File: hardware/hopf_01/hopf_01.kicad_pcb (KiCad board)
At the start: 2 copper layers, 120.2 x 120.2 mm, 257 parts, among them J1 SMA_50R, J2 SMA_50R, J3 SMA_50R, J4 SMA_50R

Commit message: updated table
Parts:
- moved ? 67.9 mm to (139.6, 69.5)
- moved ? 67.9 mm to (88.1, 117.0)
- moved ? 67.9 mm to (94.6, 128.8)
- moved ? 67.9 mm to (146.6, 74.1)
- moved ? 67.9 mm to (86.7, 62.9)
- moved ? 67.9 mm to (91.7, 56.4)
- moved ? 67.9 mm to (80.4, 72.0)
- moved ? 67.9 mm to (136.9, 117.2)
- moved ? 67.9 mm to (154.2, 56.5)
- moved ? 67.9 mm to (81.3, 74.8)
- moved ? 67.9 mm to (88.9, 55.4)
- moved ? 67.9 mm to (80.4, 61.9)
- moved ? 67.9 mm to (148.9, 114.2)
- moved ? 67.9 mm to (157.9, 125.5)
- moved ? 67.9 mm to (84.7, 123.9)
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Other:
- board size 120.2 x 120.2 mm -> 120 x 120 mm

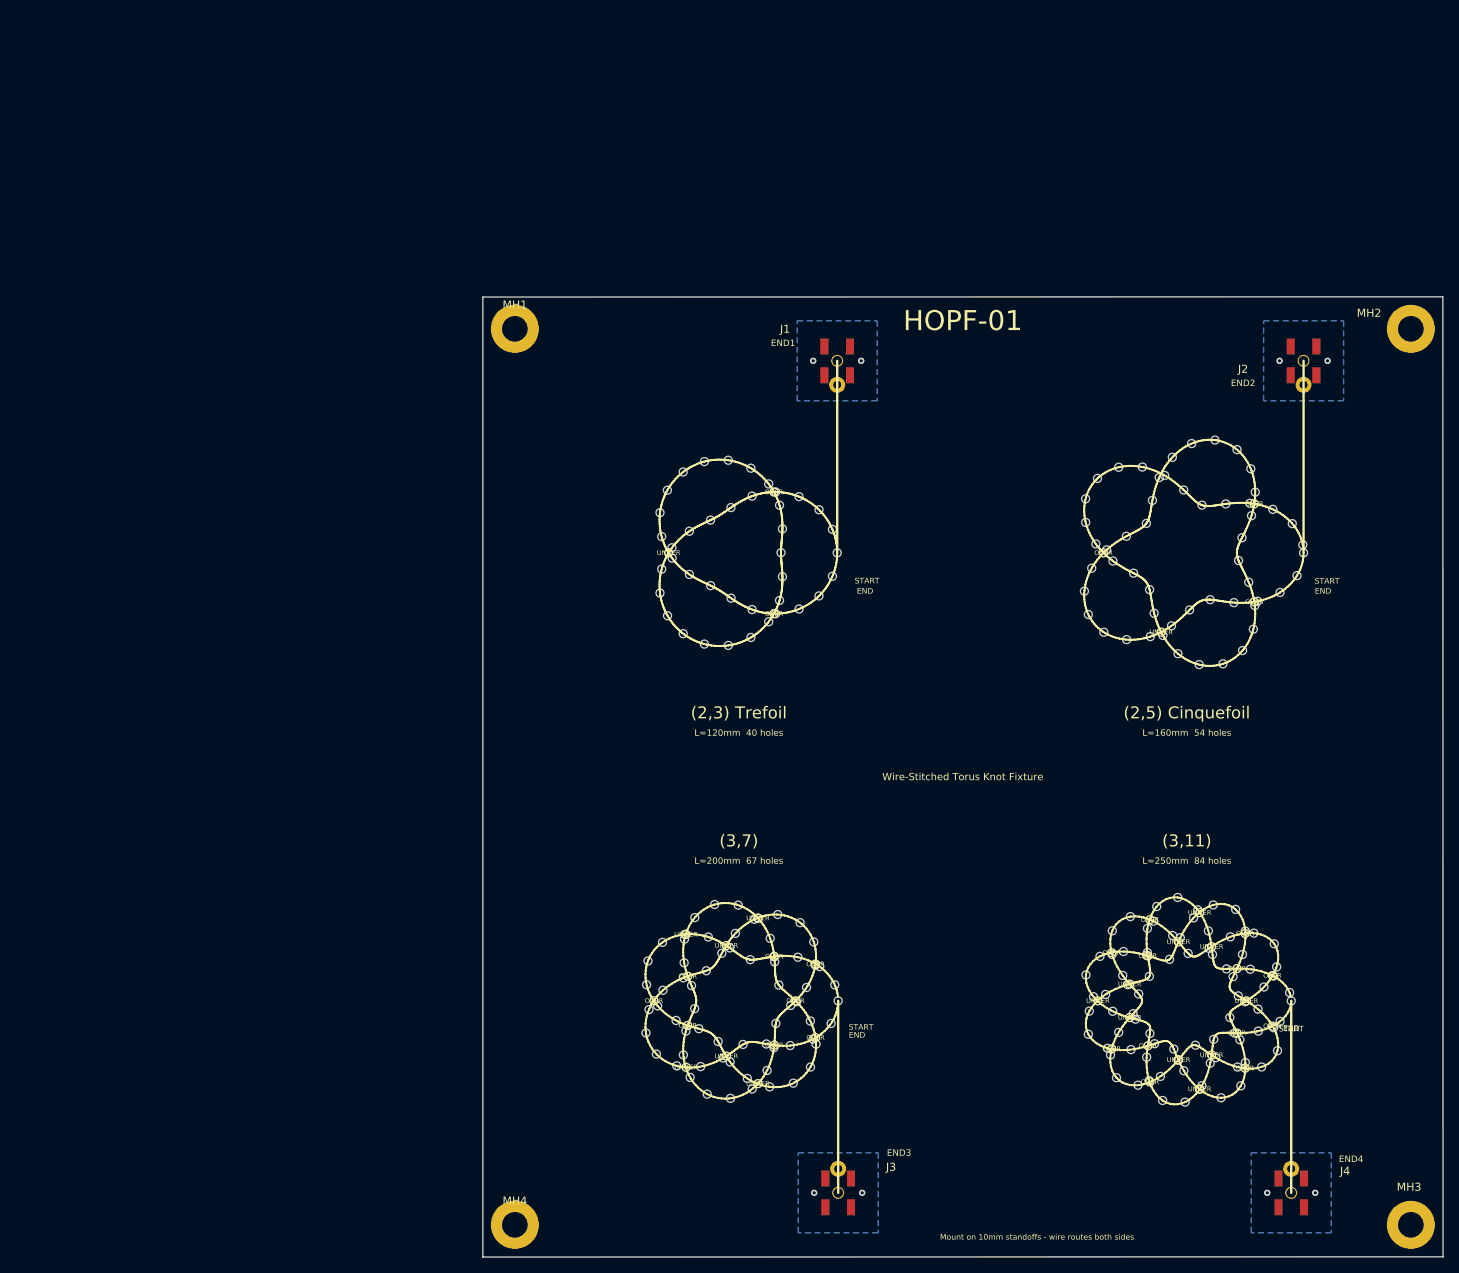
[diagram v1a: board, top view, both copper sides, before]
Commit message: updated PCB trace experiment
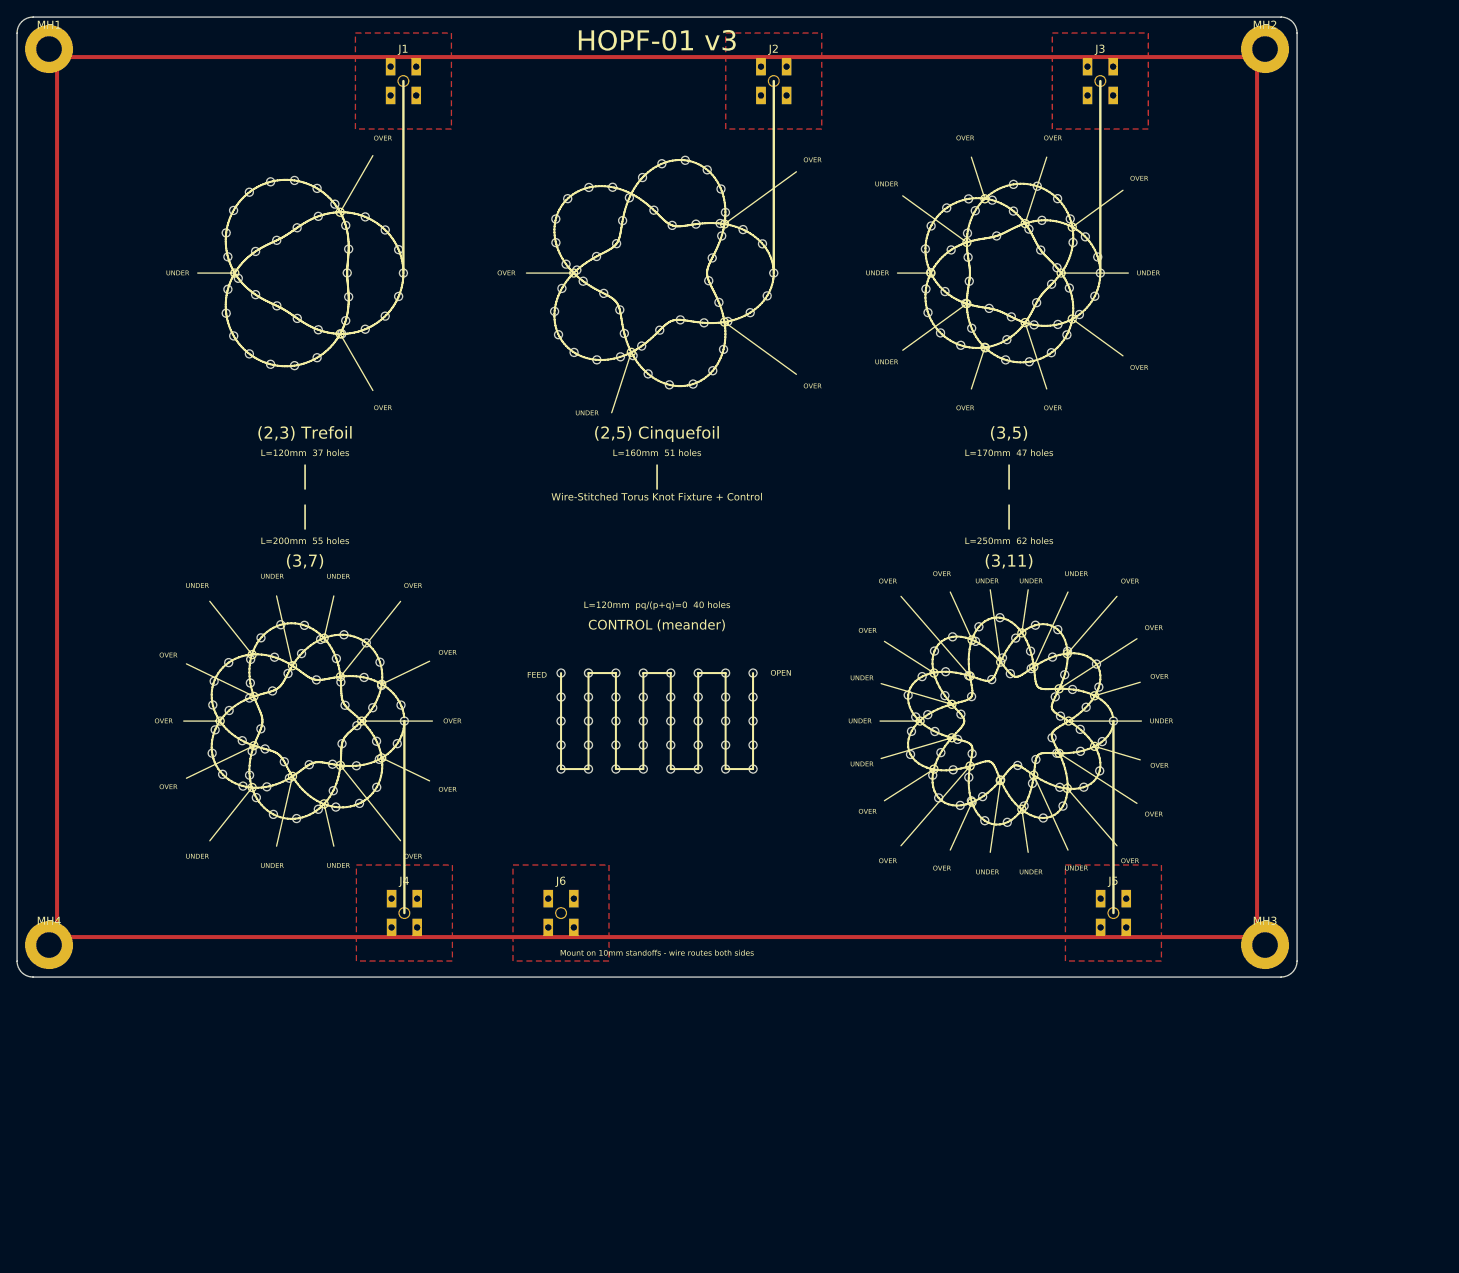
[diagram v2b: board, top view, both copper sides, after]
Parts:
- removed the ? at (139.6, 69.5)
- removed the ? at (88.1, 117.0)
- removed the ? at (83.6, 126.7)
- removed the ? at (101.9, 64.0)
- removed the ? at (94.6, 128.8)
- removed the ? at (149.8, 130.1)
- removed the ? at (137.7, 126.9)
- removed the ? at (145.9, 131.7)
- removed the ? at (146.6, 74.1)
- removed the ? at (86.7, 62.9)
- removed the ? at (96.6, 128.6)
- removed the ? at (91.7, 56.4)
- removed the ? at (144.5, 114.8)
- removed the ? at (80.4, 72.0)
- removed the ? at (142.9, 132.4)
- removed the ? at (136.9, 117.2)
- removed the ? at (154.2, 56.5)
- removed the ? at (78.7, 121.0)
- removed the ? at (81.3, 74.8)
- removed the ? at (79.0, 124.1)
- removed the ? at (88.9, 55.4)
- removed the ? at (80.4, 61.9)
- removed the ? at (148.9, 114.2)
- removed the ? at (157.9, 125.5)
- removed the ? at (94.8, 125.8)
- removed the ? at (84.7, 123.9)
- removed the ? at (83.4, 118.2)
- removed the ? at (144.4, 55.0)
- removed the ? at (145.8, 59.1)
- removed the ? at (149.1, 72.8)
- removed the ? at (85.2, 126.5)
- removed the ? at (101.9, 69.9)
- removed the ? at (83.3, 77.1)
- removed the ? at (155.1, 73.0)
- removed the ? at (89.8, 114.5)
- removed the ? at (155.9, 121.2)
- removed the ? at (84.0, 69.7)
- removed the ? at (86.3, 134.6)
- removed the ? at (84.0, 64.3)
- removed the ? at (157.0, 61.5)
- removed the ? at (136.3, 128.9)
- removed the ? at (157.6, 129.2)
- removed the ? at (85.9, 55.6)
- removed the ? at (141.6, 127.1)
- removed the ? at (145.1, 130.4)
- removed the ? at (141.5, 132.9)
- removed the ? at (95.7, 69.9)
- removed the ? at (93.7, 128.4)
- removed the ? at (151.1, 60.9)
- removed the ? at (145.4, 115.1)
- removed the ? at (99.8, 118.5)
- removed the ? at (94.6, 117.4)
- removed the ? at (138.7, 64.9)
- removed the ? at (155.2, 126.8)
- removed the ? at (97.7, 74.0)
- removed the ? at (133.6, 119.7)
- removed the ? at (154.2, 119.0)
- removed the ? at (138.7, 77.8)
- removed the ? at (99.5, 127.8)
- removed the ? at (133.4, 71.8)
- removed the ? at (152.5, 54.1)
- removed the ? at (141.2, 63.3)
- removed the ? at (153.5, 130.7)
- removed the ? at (153.5, 123.1)
- removed the ? at (94.8, 59.4)
- removed the ? at (83.3, 129.7)
- removed the ? at (83.5, 114.7)
- removed the ? at (141.2, 130.0)
- removed the ? at (80.7, 115.7)
- removed the ? at (135.1, 57.7)
- removed the ? at (91.9, 74.1)
- removed the ? at (136.2, 66.6)
- removed the ? at (86.2, 119.2)
- removed the ? at (153.5, 114.3)
- removed the ? at (101.8, 125.8)
- removed the ? at (97.7, 59.9)
- removed the ? at (152.1, 73.2)
- removed the ? at (99.9, 128.4)
- removed the ? at (141.3, 116.9)
- removed the ? at (136.9, 114.2)
- removed the ? at (155.6, 131.2)
- removed the ? at (139.8, 125.3)
- removed the ? at (155.1, 124.0)
- removed the ? at (95.3, 61.0)
- removed the ? at (80.6, 69.0)
- removed the ? at (139.2, 129.1)
- removed the ? at (79.9, 129.6)
- removed the ? at (91.9, 134.0)
- removed the ? at (100.2, 72.4)
- removed the ? at (145.1, 110.0)
- removed the ? at (144.6, 129.0)
- removed the ? at (89.1, 116.4)
- removed the ? at (153.2, 117.2)
- removed the ? at (137.7, 56.3)
- removed the ? at (153.2, 79.2)
- removed the ? at (90.1, 111.0)
- removed the ? at (149.4, 117.2)
- removed the ? at (95.2, 121.0)
- removed the ? at (151.2, 119.0)
- removed the ? at (133.6, 63.2)
- removed the ? at (160.7, 66.0)
- removed the ? at (89.3, 72.6)
- removed the ? at (138.2, 119.8)
- removed the ? at (100.2, 61.6)
- removed the ? at (133.9, 127.1)
- removed the ? at (95.1, 112.2)
- removed the ? at (93.8, 131.7)
- removed the ? at (145.1, 79.6)
- removed the ? at (84.3, 121.1)
- removed the ? at (154.8, 59.4)
- removed the ? at (149.0, 116.4)
- removed the ? at (83.3, 56.9)
- removed the ? at (87.6, 128.1)
- removed the ? at (135.4, 117.4)
- removed the ? at (148.1, 61.0)
- removed the ? at (80.6, 64.9)
- removed the ? at (150.5, 135.1)
- removed the ? at (140.1, 133.5)
- removed the ? at (149.2, 130.8)
- removed the ? at (160.8, 67.0)
- removed the ? at (98.7, 121.3)
- removed the ? at (146.0, 135.6)
- removed the ? at (136.7, 129.7)
- removed the ? at (80.1, 123.6)
- removed the ? at (146.8, 53.3)
- removed the ? at (159.1, 121.9)
- removed the ? at (137.0, 124.3)
- removed the ? at (92.2, 112.8)
- removed the ? at (153.1, 65.1)
- removed the ? at (94.8, 74.6)
- removed the ? at (147.8, 80.9)
- removed the ? at (143.2, 135.4)
- removed the ? at (141.3, 113.9)
- removed the ? at (81.9, 67.6)
- removed the ? at (94.7, 118.1)
- removed the ? at (142.8, 57.6)
- removed the ? at (97.0, 133.3)
- removed the ? at (88.9, 78.5)
- removed the ? at (134.6, 122.5)
- removed the ? at (137.0, 68.0)
- removed the ? at (142.2, 128.3)
- removed the ? at (147.3, 128.5)
- removed the ? at (84.1, 132.5)
- removed the ? at (89.1, 130.6)
- removed the ? at (99.2, 125.5)
- removed the ? at (140.2, 122.1)
- removed the ? at (96.7, 123.5)
- removed the ? at (142.0, 113.0)
- removed the ? at (152.2, 127.0)
- removed the ? at (154.6, 114.5)
- removed the ? at (141.9, 60.4)
- removed the ? at (81.9, 66.3)
- removed the ? at (139.2, 112.4)
- removed the ? at (97.6, 117.5)
- removed the ? at (84.7, 112.6)
- removed the ? at (157.2, 115.8)
- removed the ? at (82.4, 125.4)
- removed the ? at (154.5, 76.5)
- removed the ? at (136.1, 122.2)
- removed the ? at (94.0, 58.4)
- removed the ? at (152.0, 119.9)
- removed the ? at (150.7, 80.8)
- removed the ? at (91.3, 132.7)
- removed the ? at (94.1, 115.2)
- removed the ? at (154.3, 62.3)
- removed the ? at (97.4, 123.1)
- removed the ? at (138.8, 120.9)
- removed the ? at (99.6, 115.6)
- removed the ? at (144.1, 117.8)
- removed the ? at (133.6, 60.2)
- removed the ? at (86.7, 71.1)
- removed the ? at (152.9, 127.8)
- removed the ? at (157.4, 118.7)
- removed the ? at (149.7, 52.9)
- removed the ? at (92.6, 112.6)
- removed the ? at (154.0, 70.6)
- removed the ? at (141.2, 117.3)
- removed the ? at (83.4, 115.3)
- removed the ? at (80.7, 121.7)
- removed the ? at (152.3, 111.5)
- removed the ? at (91.9, 59.9)
- removed the ? at (154.7, 73.6)
- removed the ? at (154.1, 60.8)
- removed the ? at (81.3, 59.1)
- removed the ? at (142.1, 74.5)
- removed the ? at (149.6, 127.8)
- removed the ? at (91.7, 77.6)
- removed the ? at (95.3, 72.9)
- removed the ? at (100.3, 118.7)
- removed the ? at (141.6, 71.6)
- removed the ? at (102.6, 123.0)
- removed the ? at (91.6, 117.8)
- removed the ? at (142.5, 111.2)
- removed the ? at (82.5, 131.1)
- removed the ? at (95.7, 64.0)
- removed the ? at (134.0, 124.3)
- removed the ? at (149.5, 111.0)
- removed the ? at (159.3, 123.0)
- removed the ? at (88.3, 130.1)
- removed the ? at (94.0, 75.6)
- removed the ? at (97.9, 113.2)
- removed the ? at (85.4, 131.2)
- removed the ? at (102.5, 67.0)
- removed the ? at (157.1, 126.3)
- removed the ? at (99.2, 131.3)
- removed the ? at (89.2, 61.3)
- removed the ? at (90.7, 128.4)
- removed the ? at (152.6, 131.3)
- removed the ? at (157.9, 71.9)
- removed the ? at (94.1, 133.7)
- removed the ? at (159.4, 63.3)
- removed the ? at (87.2, 110.9)
- removed the ? at (134.3, 68.9)
- removed the ? at (138.3, 116.8)
- removed the ? at (143.2, 77.3)
- removed the ? at (137.4, 132.6)
- removed the ? at (133.9, 74.7)
- removed the ? at (146.4, 117.0)
- removed the ? at (148.1, 133.6)
- removed the ? at (157.1, 119.9)
- removed the ? at (89.2, 135.2)
- removed the ? at (144.3, 76.1)
- removed the ? at (78.6, 127.0)
- removed the ? at (147.6, 111.6)
- removed the ? at (141.5, 119.9)
- removed the ? at (102.2, 121.0)
- removed the ? at (153.0, 133.6)
- removed the ? at (86.4, 115.0)
- removed the ? at (78.9, 118.0)
- removed the ? at (152.7, 67.9)
- removed the ? at (147.1, 112.6)
- removed the ? at (140.7, 56.2)
- removed the ? at (134.9, 65.9)
- removed the ? at (160.0, 69.8)
- removed the ? at (135.9, 76.9)
- removed the ? at (85.9, 78.4)
- removed the ? at (143.4, 57.3)
- removed the ? at (151.7, 115.0)
- removed the ? at (139.5, 124.6)
- removed the ? at (141.7, 77.4)
- removed the ? at (147.8, 134.0)
- removed the ? at (151.6, 125.1)
- removed the ? at (152.7, 122.4)
- removed the ? at (95.5, 67.0)
- removed the ? at (83.3, 120.1)
- removed END1, END2, END3, END4: , HOPF01:AnchorPad
- added ?: , HOPF01:StitchHole, F.Cu at (74.9, 91.0)
- added ?: , HOPF01:StitchHole, F.Cu at (72.5, 42.8)
- added ?: , HOPF01:StitchHole, F.Cu at (68.0, 88.0)
- added ?: , HOPF01:StitchHole, F.Cu at (37.7, 24.9)
- added ?: , HOPF01:StitchHole, F.Cu at (129.3, 33.4)
- added ?: , HOPF01:StitchHole, F.Cu at (31.9, 84.2)
- added ?: , HOPF01:StitchHole, F.Cu at (68.1, 33.9)
- added ?: , HOPF01:StitchHole, F.Cu at (39.4, 93.4)
- added ?: , HOPF01:StitchHole, F.Cu at (29.9, 97.6)
- added ?: , HOPF01:StitchHole, F.Cu at (124.5, 24.3)
- added ?: , HOPF01:StitchHole, F.Cu at (32.5, 27.9)
- added ?: , HOPF01:StitchHole, F.Cu at (46.0, 37.4)
- added ?: , HOPF01:StitchHole, F.Cu at (68.0, 94.0)
- added ?: , HOPF01:StitchHole, F.Cu at (116.0, 34.3)
- added ?: , HOPF01:StitchHole, F.Cu at (116.0, 84.8)
- added ?: , HOPF01:StitchHole, F.Cu at (118.0, 87.1)
- added ?: , HOPF01:StitchHole, F.Cu at (127.4, 35.7)
- added ?: , HOPF01:StitchHole, F.Cu at (129.8, 85.0)
- added ?: , HOPF01:StitchHole, F.Cu at (131.3, 79.3)
- added ?: , HOPF01:StitchHole, F.Cu at (29.1, 85.1)
- added ?: , HOPF01:StitchHole, F.Cu at (39.5, 96.7)
- added ?: , HOPF01:StitchHole, F.Cu at (40.6, 90.8)
- added ?: , HOPF01:StitchHole, F.Cu at (130.0, 92.0)
- added ?: , HOPF01:StitchHole, F.Cu at (70.8, 33.0)
- added ?: , HOPF01:StitchHole, F.Cu at (119.0, 82.3)
- added ?: , HOPF01:StitchHole, F.Cu at (79.6, 24.1)
- added ?: , HOPF01:StitchHole, F.Cu at (84.9, 25.9)
- added ?: , HOPF01:StitchHole, F.Cu at (70.0, 31.6)
- added ?: , HOPF01:StitchHole, F.Cu at (132.9, 89.0)
- added ?: , HOPF01:StitchHole, F.Cu at (27.1, 39.9)
- added ?: , HOPF01:StitchHole, F.Cu at (85.1, 82.0)
- added ?: , HOPF01:StitchHole, F.Cu at (40.9, 77.2)
- added ?: , HOPF01:StitchHole, F.Cu at (114.7, 89.3)
- added ?: , HOPF01:StitchHole, F.Cu at (115.4, 39.5)
- added ?: , HOPF01:StitchHole, F.Cu at (78.1, 41.1)
- added ?: , HOPF01:StitchHole, F.Cu at (32.0, 99.7)
- added ?: , HOPF01:StitchHole, F.Cu at (122.9, 95.4)
- added ?: , HOPF01:StitchHole, F.Cu at (24.5, 86.0)
- added ?: , HOPF01:StitchHole, F.Cu at (74.4, 21.3)
- added ?: , HOPF01:StitchHole, F.Cu at (41.0, 86.0)
- added ?: , HOPF01:StitchHole, F.Cu at (37.7, 39.1)
- added ?: , HOPF01:StitchHole, F.Cu at (67.3, 25.2)
- added ?: , HOPF01:StitchHole, F.Cu at (69.6, 41.9)
- added ?: , HOPF01:StitchHole, F.Cu at (26.4, 30.0)
- added ?: , HOPF01:StitchHole, F.Cu at (34.9, 100.2)
- added ?: , HOPF01:StitchHole, F.Cu at (68.0, 82.0)
- added ?: , HOPF01:StitchHole, F.Cu at (111.8, 89.3)
- added ?: , HOPF01:StitchHole, F.Cu at (82.9, 37.8)
- added ?: , HOPF01:StitchHole, F.Cu at (85.1, 91.0)
- added ?: , HOPF01:StitchHole, F.Cu at (71.4, 91.0)
- added ?: , HOPF01:StitchHole, F.Cu at (73.3, 34.5)
- added ?: , HOPF01:StitchHole, F.Cu at (130.1, 38.4)
- added ?: , HOPF01:StitchHole, F.Cu at (78.3, 88.0)
- added ?: , HOPF01:StitchHole, F.Cu at (81.7, 94.0)
- added ?: , HOPF01:StitchHole, F.Cu at (33.4, 93.1)
- added ?: , HOPF01:StitchHole, F.Cu at (129.4, 90.1)
- added ?: , HOPF01:StitchHole, F.Cu at (121.8, 82.8)
- added ?: , HOPF01:StitchHole, F.Cu at (43.5, 25.0)
- added ?: , HOPF01:StitchHole, F.Cu at (87.9, 25.8)
- added ?: , HOPF01:StitchHole, F.Cu at (37.4, 82.9)
- added ?: , HOPF01:StitchHole, F.Cu at (90.8, 26.6)
- added ?: , HOPF01:StitchHole, F.Cu at (134.7, 34.9)
- added ?: , HOPF01:StitchHole, F.Cu at (67.4, 28.2)
- added ?: , HOPF01:StitchHole, F.Cu at (88.6, 91.0)
- added ?: , HOPF01:StitchHole, F.Cu at (28.2, 90.5)
- added ?: , HOPF01:StitchHole, F.Cu at (81.7, 88.0)
- added ?: , HOPF01:StitchHole, F.Cu at (130.4, 87.4)
- added ?: , HOPF01:StitchHole, F.Cu at (119.3, 38.9)
- added ?: , HOPF01:StitchHole, F.Cu at (76.5, 22.6)
- added ?: , HOPF01:StitchHole, F.Cu at (111.7, 92.2)
- added ?: , HOPF01:StitchHole, F.Cu at (118.0, 41.0)
- added ?: , HOPF01:StitchHole, F.Cu at (29.0, 42.1)
- added ?: , HOPF01:StitchHole, F.Cu at (120.2, 76.2)
- added ?: , HOPF01:StitchHole, F.Cu at (29.4, 91.8)
- added ?: , HOPF01:StitchHole, F.Cu at (81.7, 85.0)
- added ?: , HOPF01:StitchHole, F.Cu at (114.3, 26.1)
- added ?: , HOPF01:StitchHole, F.Cu at (114.2, 31.9)
- added ?: , HOPF01:StitchHole, F.Cu at (45.3, 92.8)
- added ?: , HOPF01:StitchHole, F.Cu at (113.1, 82.4)
- added ?: , HOPF01:StitchHole, F.Cu at (41.1, 26.0)
- added ?: , HOPF01:StitchHole, F.Cu at (126.7, 79.3)
- added ?: , HOPF01:StitchHole, F.Cu at (48.3, 32.0)
- added ?: , HOPF01:StitchHole, F.Cu at (45.6, 83.6)
- added ?: , HOPF01:StitchHole, F.Cu at (75.9, 39.6)
- added ?: , HOPF01:StitchHole, F.Cu at (130.3, 96.3)
- added ?: , HOPF01:StitchHole, F.Cu at (123.7, 40.3)
- added ?: , HOPF01:StitchHole, F.Cu at (31.2, 96.2)
- added ?: , HOPF01:StitchHole, F.Cu at (132.9, 91.8)
- added ?: , HOPF01:StitchHole, F.Cu at (114.7, 79.2)
- added ?: , HOPF01:StitchHole, F.Cu at (119.0, 33.0)
- added ?: , HOPF01:StitchHole, F.Cu at (127.1, 38.5)
- added ?: , HOPF01:StitchHole, F.Cu at (88.0, 21.5)
- added ?: , HOPF01:StitchHole, F.Cu at (113.5, 29.0)
- added ?: , HOPF01:StitchHole, F.Cu at (40.6, 39.6)
- added ?: , HOPF01:StitchHole, F.Cu at (45.0, 96.3)
- added ?: , HOPF01:StitchHole, F.Cu at (32.2, 80.0)
- added ?: , HOPF01:StitchHole, F.Cu at (88.6, 88.0)
- added ?: , HOPF01:StitchHole, F.Cu at (86.9, 30.1)
- added ?: , HOPF01:StitchHole, F.Cu at (135.4, 32.0)
- added ?: , HOPF01:StitchHole, F.Cu at (94.6, 32.0)
- added ?: , HOPF01:StitchHole, F.Cu at (44.9, 90.5)
- added ?: , HOPF01:StitchHole, F.Cu at (78.9, 44.6)
- added ?: , HOPF01:StitchHole, F.Cu at (128.3, 100.1)
- added ?: , HOPF01:StitchHole, F.Cu at (113.9, 36.9)
- added ?: , HOPF01:StitchHole, F.Cu at (114.5, 94.8)
- added ?: , HOPF01:StitchHole, F.Cu at (41.5, 29.0)
- added ?: , HOPF01:StitchHole, F.Cu at (41.1, 38.0)
- added ?: , HOPF01:StitchHole, F.Cu at (83.5, 17.9)
- added ?: , HOPF01:StitchHole, F.Cu at (34.0, 95.1)
- added ?: , HOPF01:StitchHole, F.Cu at (113.8, 87.2)
- added ?: , HOPF01:StitchHole, F.Cu at (47.5, 90.8)
- added ?: , HOPF01:StitchHole, F.Cu at (91.6, 37.0)
- added ?: , HOPF01:StitchHole, F.Cu at (118.9, 22.7)
- added ?: , HOPF01:StitchHole, F.Cu at (124.3, 37.5)
- added ?: , HOPF01:StitchHole, F.Cu at (130.1, 22.7)
- added ?: , HOPF01:StitchHole, F.Cu at (124.2, 82.1)
- added ?: , HOPF01:StitchHole, F.Cu at (35.0, 26.3)
- added ?: , HOPF01:StitchHole, F.Cu at (88.3, 41.5)
- added ?: , HOPF01:StitchHole, F.Cu at (78.3, 94.0)
- added ?: , HOPF01:StitchHole, F.Cu at (121.0, 100.5)
- added ?: , HOPF01:StitchHole, F.Cu at (75.4, 42.5)
- added ?: , HOPF01:StitchHole, F.Cu at (30.5, 77.6)
- added ?: , HOPF01:StitchHole, F.Cu at (74.9, 94.0)
- added ?: , HOPF01:StitchHole, F.Cu at (47.7, 29.1)
- added ?: , HOPF01:StitchHole, F.Cu at (130.7, 98.6)
- added ?: , HOPF01:StitchHole, F.Cu at (111.4, 84.8)
- added ?: , HOPF01:StitchHole, F.Cu at (25.7, 94.7)
- added ?: , HOPF01:StitchHole, F.Cu at (26.1, 27.0)
- added ?: , HOPF01:StitchHole, F.Cu at (135.1, 30.0)
- added ?: , HOPF01:StitchHole, F.Cu at (130.0, 31.3)
- added ?: , HOPF01:StitchHole, F.Cu at (74.9, 85.0)
- added ?: , HOPF01:StitchHole, F.Cu at (44.5, 86.3)
- added ?: , HOPF01:StitchHole, F.Cu at (39.9, 80.2)
- added ?: , HOPF01:StitchHole, F.Cu at (39.7, 23.4)
- added ?: , HOPF01:StitchHole, F.Cu at (31.7, 43.4)
- added ?: , HOPF01:StitchHole, F.Cu at (29.2, 83.2)
- added ?: , HOPF01:StitchHole, F.Cu at (29.2, 80.3)
- added ?: , HOPF01:StitchHole, F.Cu at (68.8, 22.7)
- added ?: , HOPF01:StitchHole, F.Cu at (92.0, 91.0)
- added ?: , HOPF01:StitchHole, F.Cu at (74.9, 88.0)
- added ?: , HOPF01:StitchHole, F.Cu at (34.7, 20.4)
- added ?: , HOPF01:StitchHole, F.Cu at (92.0, 85.0)
- added ?: , HOPF01:StitchHole, F.Cu at (29.0, 21.9)
- added ?: , HOPF01:StitchHole, F.Cu at (92.0, 82.0)
- added ?: , HOPF01:StitchHole, F.Cu at (26.5, 80.7)
- added ?: , HOPF01:StitchHole, F.Cu at (134.9, 80.9)
- added ?: , HOPF01:StitchHole, F.Cu at (113.6, 34.0)
- added ?: , HOPF01:StitchHole, F.Cu at (37.5, 42.6)
- added ?: , HOPF01:StitchHole, F.Cu at (119.8, 24.2)
- added ?: , HOPF01:StitchHole, F.Cu at (92.0, 88.0)
- added ?: , HOPF01:StitchHole, F.Cu at (88.1, 27.4)
- added ?: , HOPF01:StitchHole, F.Cu at (123.2, 80.1)
- added ?: , HOPF01:StitchHole, F.Cu at (71.4, 94.0)
- added ?: , HOPF01:StitchHole, F.Cu at (41.3, 32.0)
- added ?: , HOPF01:StitchHole, F.Cu at (47.7, 34.9)
- added ?: , HOPF01:StitchHole, F.Cu at (34.7, 43.6)
- added ?: , HOPF01:StitchHole, F.Cu at (137.0, 88.0)
- added ?: , HOPF01:StitchHole, F.Cu at (68.0, 85.0)
- added ?: , HOPF01:StitchHole, F.Cu at (119.4, 92.1)
- added ?: , HOPF01:StitchHole, F.Cu at (29.8, 29.3)
- added ?: , HOPF01:StitchHole, F.Cu at (132.8, 37.2)
- added ?: , HOPF01:StitchHole, F.Cu at (31.0, 91.5)
- added ?: , HOPF01:StitchHole, F.Cu at (29.8, 34.7)
- added ?: , HOPF01:StitchHole, F.Cu at (24.6, 83.0)
- added ?: , HOPF01:StitchHole, F.Cu at (127.5, 21.1)
- added ?: , HOPF01:StitchHole, F.Cu at (71.4, 85.0)
- added ?: , HOPF01:StitchHole, F.Cu at (80.3, 39.1)
- added ?: , HOPF01:StitchHole, F.Cu at (33.9, 82.1)
- added ?: , HOPF01:StitchHole, F.Cu at (88.5, 24.4)
- added ?: , HOPF01:StitchHole, F.Cu at (87.0, 44.2)
- added ?: , HOPF01:StitchHole, F.Cu at (42.4, 93.6)
- added ?: , HOPF01:StitchHole, F.Cu at (117.0, 94.1)
- added ?: , HOPF01:StitchHole, F.Cu at (118.6, 35.8)
- added ?: , HOPF01:StitchHole, F.Cu at (121.5, 36.4)
- added ?: , HOPF01:StitchHole, F.Cu at (127.4, 92.8)
- added ?: , HOPF01:StitchHole, F.Cu at (124.8, 77.6)
- added ?: , HOPF01:StitchHole, F.Cu at (26.1, 37.0)
- added ?: , HOPF01:StitchHole, F.Cu at (33.0, 76.0)
- added ?: , HOPF01:StitchHole, F.Cu at (131.0, 82.2)
- added ?: , HOPF01:StitchHole, F.Cu at (77.0, 42.3)
- added ?: , HOPF01:StitchHole, F.Cu at (115.5, 91.9)
- added ?: , HOPF01:StitchHole, F.Cu at (81.7, 82.0)
- added ?: , HOPF01:StitchHole, F.Cu at (43.5, 39.0)
- added ?: , HOPF01:StitchHole, F.Cu at (131.9, 84.1)
- added ?: , HOPF01:StitchHole, F.Cu at (43.7, 78.2)
- added ?: , HOPF01:StitchHole, F.Cu at (118.8, 27.0)
- added ?: , HOPF01:StitchHole, F.Cu at (88.6, 82.0)
- added ?: , HOPF01:StitchHole, F.Cu at (32.5, 36.1)
- added ?: , HOPF01:StitchHole, F.Cu at (85.1, 88.0)
- added ?: , HOPF01:StitchHole, F.Cu at (128.0, 29.1)
- added ?: , HOPF01:StitchHole, F.Cu at (67.2, 36.8)
- added ?: , HOPF01:StitchHole, F.Cu at (46.0, 26.6)
- added ?: , HOPF01:StitchHole, F.Cu at (116.9, 77.5)
- added ?: , HOPF01:StitchHole, F.Cu at (43.4, 82.5)
- added ?: , HOPF01:StitchHole, F.Cu at (123.8, 100.7)
- added ?: , HOPF01:StitchHole, F.Cu at (31.7, 20.6)
- added ?: , HOPF01:StitchHole, F.Cu at (81.7, 91.0)
- added ?: , HOPF01:StitchHole, F.Cu at (37.9, 77.8)
- added ?: , HOPF01:StitchHole, F.Cu at (125.1, 93.5)
- added ?: , HOPF01:StitchHole, F.Cu at (71.5, 21.3)
- added ?: , HOPF01:StitchHole, F.Cu at (116.2, 23.9)
- added ?: , HOPF01:StitchHole, F.Cu at (126.8, 81.4)
- added ?: , HOPF01:StitchHole, F.Cu at (36.5, 93.5)
- added ?: , HOPF01:StitchHole, F.Cu at (71.4, 82.0)
- added ?: , HOPF01:StitchHole, F.Cu at (80.6, 18.3)
- added ?: , HOPF01:StitchHole, F.Cu at (35.9, 76.0)
- added ?: , HOPF01:StitchHole, F.Cu at (37.5, 21.4)
- added ?: , HOPF01:StitchHole, F.Cu at (75.7, 25.4)
- added ?: , HOPF01:StitchHole, F.Cu at (85.9, 38.2)
- added ?: , HOPF01:StitchHole, F.Cu at (112.3, 87.5)
- added ?: , HOPF01:StitchHole, F.Cu at (42.5, 88.6)
- added ?: , HOPF01:StitchHole, F.Cu at (119.8, 78.0)
- added ?: , HOPF01:StitchHole, F.Cu at (131.5, 33.9)
- added ?: , HOPF01:StitchHole, F.Cu at (27.7, 32.7)
- added ?: , HOPF01:StitchHole, F.Cu at (78.3, 85.0)
- added ?: , HOPF01:StitchHole, F.Cu at (68.0, 91.0)
- added ?: , HOPF01:StitchHole, F.Cu at (128.1, 25.4)
- added ?: , HOPF01:StitchHole, F.Cu at (67.7, 39.7)
- added ?: , HOPF01:StitchHole, F.Cu at (35.6, 79.6)
- added ?: , HOPF01:StitchHole, F.Cu at (86.3, 19.1)
- added ?: , HOPF01:StitchHole, F.Cu at (24.4, 92.0)
- added ?: , HOPF01:StitchHole, F.Cu at (125.9, 98.6)
- added ?: , HOPF01:StitchHole, F.Cu at (37.7, 99.0)
- added ?: , HOPF01:StitchHole, F.Cu at (88.6, 85.0)
- added ?: , HOPF01:StitchHole, F.Cu at (78.3, 91.0)
- added ?: , HOPF01:StitchHole, F.Cu at (41.5, 35.0)
- added ?: , HOPF01:StitchHole, F.Cu at (78.2, 20.1)
- added ?: , HOPF01:StitchHole, F.Cu at (48.0, 86.0)
- added ?: , HOPF01:StitchHole, F.Cu at (117.6, 90.3)
- added ?: , HOPF01:StitchHole, F.Cu at (85.1, 94.0)
- added ?: , HOPF01:StitchHole, F.Cu at (74.9, 82.0)
- added ?: , HOPF01:StitchHole, F.Cu at (68.6, 30.9)
- added ?: , HOPF01:StitchHole, F.Cu at (124.6, 20.9)
- added ?: , HOPF01:StitchHole, F.Cu at (131.6, 25.2)
- added ?: , HOPF01:StitchHole, F.Cu at (120.7, 97.4)
- added ?: , HOPF01:StitchHole, F.Cu at (132.0, 28.2)
- added ?: , HOPF01:StitchHole, F.Cu at (119.0, 95.0)
- added ?: , HOPF01:StitchHole, F.Cu at (93.8, 34.9)
- added ?: , HOPF01:StitchHole, F.Cu at (118.9, 30.0)
- added ?: , HOPF01:StitchHole, F.Cu at (123.6, 42.9)
- added ?: , HOPF01:StitchHole, F.Cu at (133.6, 86.3)
- added ?: , HOPF01:StitchHole, F.Cu at (126.5, 43.1)
- added ?: , HOPF01:StitchHole, F.Cu at (129.4, 80.0)
- added ?: , HOPF01:StitchHole, F.Cu at (131.2, 39.7)
- added ?: , HOPF01:StitchHole, F.Cu at (133.5, 27.5)
- added ?: , HOPF01:StitchHole, F.Cu at (26.4, 34.0)
- added ?: , HOPF01:StitchHole, F.Cu at (126.5, 26.5)
- added ?: , HOPF01:StitchHole, F.Cu at (127.3, 76.0)
- added ?: , HOPF01:StitchHole, F.Cu at (92.0, 94.0)
- added ?: , HOPF01:StitchHole, F.Cu at (86.5, 33.0)
- added ?: , HOPF01:StitchHole, F.Cu at (130.1, 76.6)
- added ?: , HOPF01:StitchHole, F.Cu at (29.1, 94.8)
- added ?: , HOPF01:StitchHole, F.Cu at (48.4, 88.0)
- added ?: , HOPF01:StitchHole, F.Cu at (27.1, 24.2)
- added ?: , HOPF01:StitchHole, F.Cu at (87.7, 35.7)
- added ?: , HOPF01:StitchHole, F.Cu at (121.9, 22.9)
- added ?: , HOPF01:StitchHole, F.Cu at (116.8, 29.1)
- added ?: , HOPF01:StitchHole, F.Cu at (74.9, 28.3)
- added ?: , HOPF01:StitchHole, F.Cu at (35.0, 37.7)
- added ?: , HOPF01:StitchHole, F.Cu at (81.9, 26.0)
- added ?: , HOPF01:StitchHole, F.Cu at (85.1, 85.0)
- added ?: , HOPF01:StitchHole, F.Cu at (117.9, 98.5)
- added ?: , HOPF01:StitchHole, F.Cu at (26.5, 86.7)
- added ?: , HOPF01:StitchHole, F.Cu at (116.1, 81.8)
- added ?: , HOPF01:StitchHole, F.Cu at (28.2, 96.1)
- added ?: , HOPF01:StitchHole, F.Cu at (39.9, 98.8)
- added ?: , HOPF01:StitchHole, F.Cu at (88.8, 38.1)
- added ?: , HOPF01:StitchHole, F.Cu at (88.6, 94.0)
- added ?: , HOPF01:StitchHole, F.Cu at (126.9, 95.8)
- added ?: , HOPF01:StitchHole, F.Cu at (75.3, 36.6)
- added ?: , HOPF01:StitchHole, F.Cu at (78.3, 82.0)
- added ?: , HOPF01:StitchHole, F.Cu at (93.2, 28.4)
- added ?: , HOPF01:StitchHole, F.Cu at (84.5, 45.9)
- added ?: , HOPF01:StitchHole, F.Cu at (24.8, 89.1)
- added ?: , HOPF01:StitchHole, F.Cu at (45.4, 80.6)
- added ?: , HOPF01:StitchHole, F.Cu at (81.5, 46.0)
- added ?: , HOPF01:StitchHole, F.Cu at (135.7, 90.6)
- added ?: , HOPF01:StitchHole, F.Cu at (119.3, 84.9)
- added ?: , HOPF01:StitchHole, F.Cu at (40.5, 83.1)
- added ?: , HOPF01:StitchHole, F.Cu at (42.8, 98.3)
- added ?: , HOPF01:StitchHole, F.Cu at (30.5, 89.0)
- added ?: , HOPF01:StitchHole, F.Cu at (129.3, 42.0)
- added ?: , HOPF01:StitchHole, F.Cu at (115.2, 97.6)
- added ?: , HOPF01:StitchHole, F.Cu at (133.3, 96.3)
- added ?: , HOPF01:StitchHole, F.Cu at (122.9, 75.1)
- added ?: , HOPF01:StitchHole, F.Cu at (135.3, 94.2)
- added ?: , HOPF01:StitchHole, F.Cu at (121.0, 41.3)
- added ?: , HOPF01:StitchHole, F.Cu at (135.2, 83.8)
- added ?: , HOPF01:StitchHole, F.Cu at (72.4, 29.9)
- added ?: , HOPF01:StitchHole, F.Cu at (122.4, 27.4)
- added ?: , HOPF01:StitchHole, F.Cu at (71.4, 88.0)
- added ?: , HOPF01:StitchHole, F.Cu at (119.3, 98.0)
- added J5: SMA_50R, HOPF01:SMA_PanelMount, F.Cu at (137.0, 112.0)
- added J6: SMA_50R, HOPF01:SMA_PanelMount, F.Cu at (68.0, 112.0)
- J1, J2, J3, J4: footprint HOPF01:SMA_EdgeLaunch -> HOPF01:SMA_PanelMount
- moved J3 142.8 mm to (135.4, 8.00)
- moved J4 116.2 mm to (48.4, 112.0)
- moved J2 74.9 mm to (94.6, 8.00)
- moved MH4 67.9 mm to (4.00, 116.0)
- moved MH1 67.9 mm to (4.00, 4.00)
- moved J1 64.5 mm to (48.3, 8.00)
- moved MH3 39.4 mm to (156.0, 116.0)
- moved MH2 39.4 mm to (156.0, 4.00)
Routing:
- net GND: track 0.00 -> 520.0 mm, vias 8 -> 0
- added copper zone on F.Cu, net GND
- removed copper zone on B.Cu, net GND
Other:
- board size 120 x 120 mm -> 160 x 120 mm
- board text added: "(3,5)"
- board text added: "CONTROL (meander)"
- board text added: "FEED"
- board text added: "HOPF-01 v3"
- board text added: "L=120mm 37 holes"
- board text added: "L=120mm pq/(p+q)=0 40 holes"
- board text added: "L=160mm 51 holes"
- board text added: "L=170mm 47 holes"
- board text added: "L=200mm 55 holes"
- board text added: "L=250mm 62 holes"
- board text added: "OPEN"
- board text added: "Wire-Stitched Torus Knot Fixture + Control"
- board text removed: "END"
- board text removed: "HOPF-01"
- board text removed: "L=120mm 40 holes"
- board text removed: "L=160mm 54 holes"
- board text removed: "L=200mm 67 holes"
- board text removed: "L=250mm 84 holes"
- board text removed: "START"
- board text removed: "Wire-Stitched Torus Knot Fixture"
